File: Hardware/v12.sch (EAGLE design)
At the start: 82 parts, among them IC1 LM324D, IC2 m328p, IC3 REG1117, IC4 OPA336U, J1 22-27-2081-08, J2 22-27-2031-03

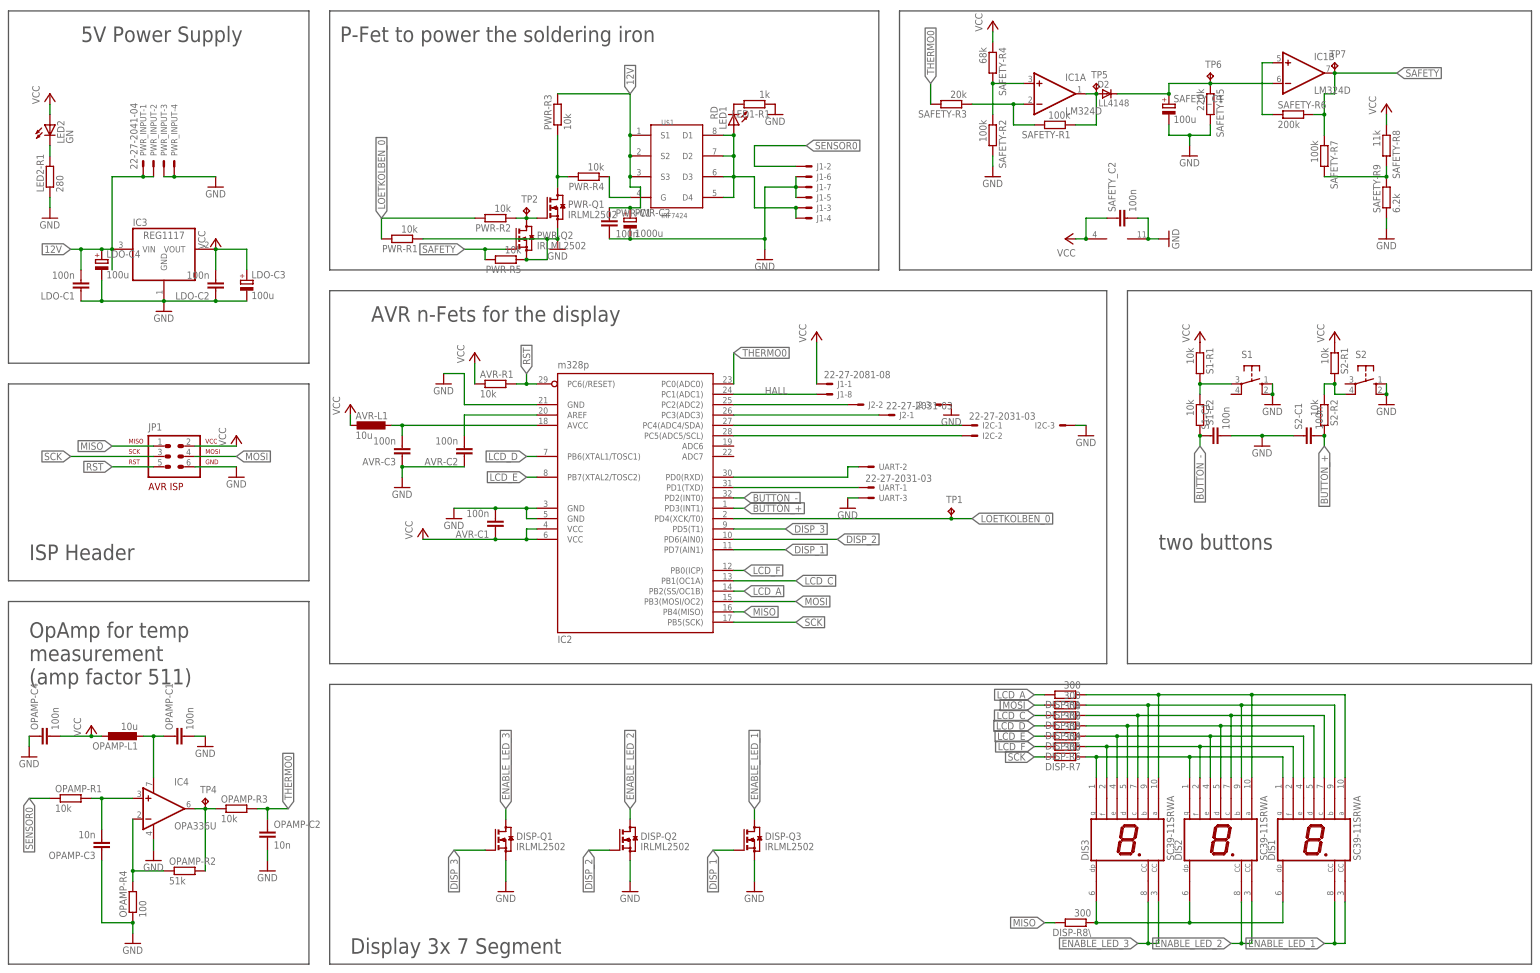
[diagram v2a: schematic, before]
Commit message: added silk screen to test points and optimized ground connections
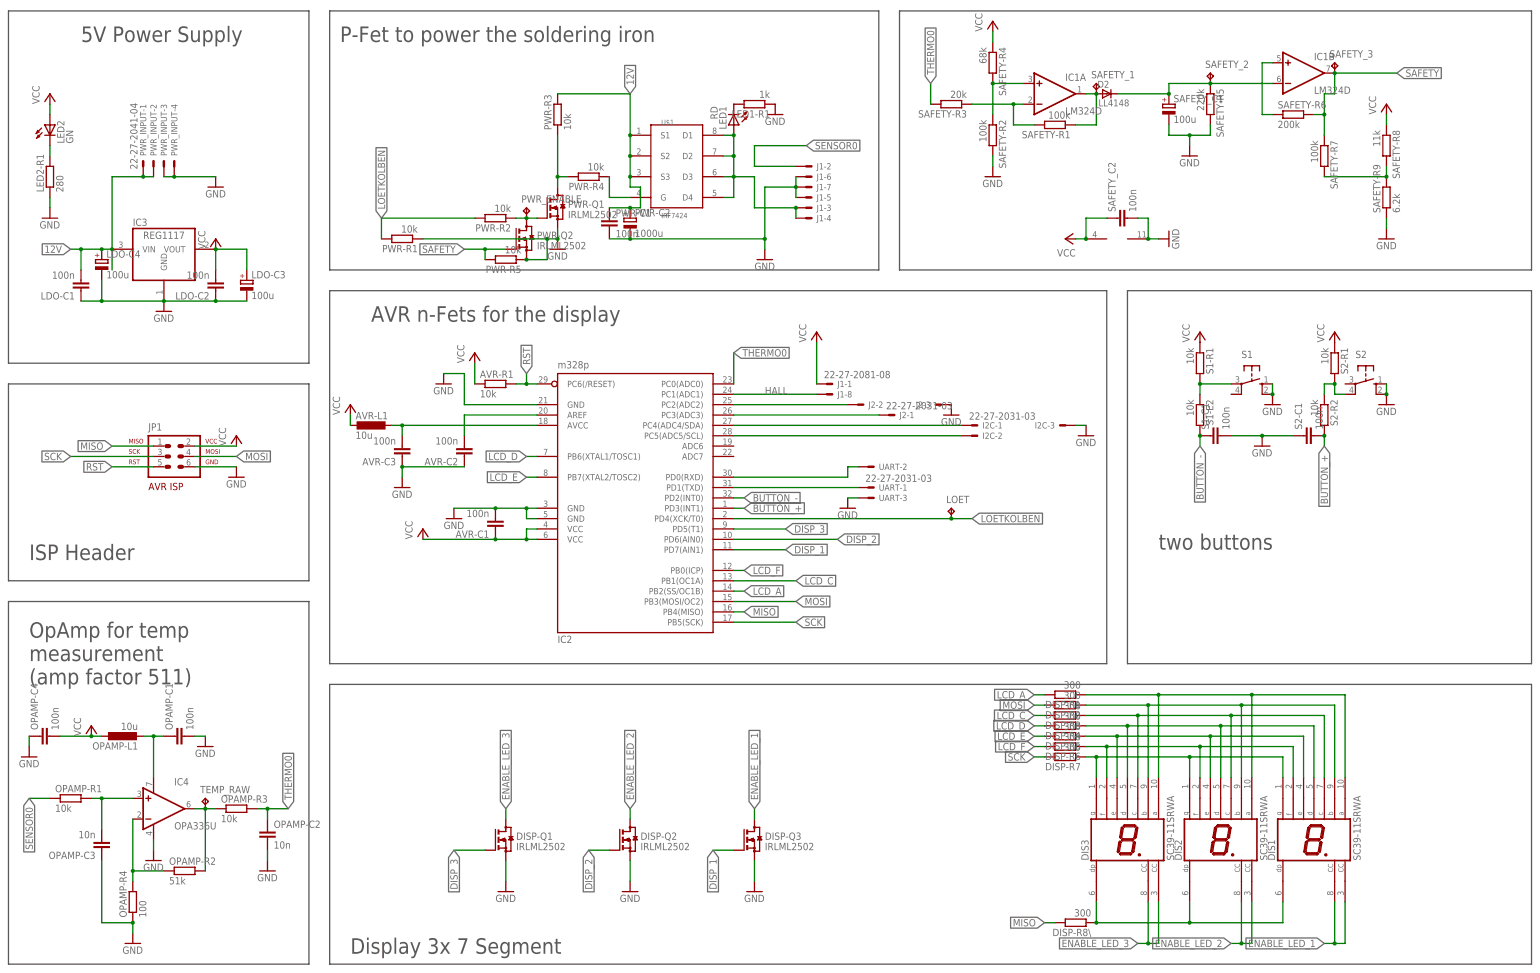
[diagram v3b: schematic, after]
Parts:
- renumbered TP1 to LOET, TP2 to PWR_ENABLE, TP4 to TEMP_RAW, TP5 to SAFETY_1, TP6 to SAFETY_2, TP7 to SAFETY_3
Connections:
- net LOETKOLBEN_0 renamed LOETKOLBEN
- net N$10 renamed TX
- net N$13 renamed PC2
- net N$2 renamed SDA
- net N$3 renamed PC3
- net N$4 renamed SCL
- net N$9 renamed RX
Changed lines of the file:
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@@
 <part name="J2" library="con-molex" deviceset="22-?-03" device="27-2031"/>
 <part name="GND28" library="supply1" deviceset="GND" device=""/>
-<part name="TP1" library="testpad" deviceset="TP" device="B1,27"/>
-<part name="TP2" library="testpad" deviceset="TP" device="B1,27"/>
-<part name="TP4" library="testpad" deviceset="TP" device="B1,27"/>
-<part name="TP5" library="testpad" deviceset="TP" device="B1,27"/>
-<part name="TP6" library="testpad" deviceset="TP" device="B1,27"/>
-<part name="TP7" library="testpad" deviceset="TP" device="B1,27"/>
+<part name="LOET" library="testpad" deviceset="TP" device="B1,27"/>
+<part name="PWR_ENABLE" library="testpad" deviceset="TP" device="B1,27"/>
+<part name="TEMP_RAW" library="testpad" deviceset="TP" device="B1,27"/>
+<part name="SAFETY_1" library="testpad" deviceset="TP" device="B1,27"/>
+<part name="SAFETY_2" library="testpad" deviceset="TP" device="B1,27"/>
+<part name="SAFETY_3" library="testpad" deviceset="TP" device="B1,27"/>
 <part name="D2" library="_hhn_diodes_smd" deviceset="LL4148" device=""/>
 </parts>
@@
 <instance part="J2" gate="-3" x="254" y="165.1" rot="R180"/>
 <instance part="GND28" gate="1" x="256.54" y="162.56"/>
-<instance part="TP1" gate="G$1" x="256.54" y="139.7"/>
-<instance part="TP2" gate="G$1" x="152.4" y="213.36"/>
-<instance part="TP4" gate="G$1" x="73.66" y="68.58"/>
-<instance part="TP5" gate="G$1" x="292.1" y="243.84"/>
-<instance part="TP6" gate="G$1" x="320.04" y="246.38"/>
-<instance part="TP7" gate="G$1" x="350.52" y="248.92"/>
+<instance part="LOET" gate="G$1" x="256.54" y="139.7"/>
+<instance part="PWR_ENABLE" gate="G$1" x="152.4" y="213.36"/>
+<instance part="TEMP_RAW" gate="G$1" x="73.66" y="68.58"/>
+<instance part="SAFETY_1" gate="G$1" x="292.1" y="243.84"/>
+<instance part="SAFETY_2" gate="G$1" x="320.04" y="246.38"/>
+<instance part="SAFETY_3" gate="G$1" x="350.52" y="248.92"/>
 <instance part="D2" gate="G$1" x="294.64" y="241.3"/>
 </instances>
@@
 </segment>
 </net>
-<net name="LOETKOLBEN_0" class="0">
+<net name="LOETKOLBEN" class="0">
 <segment>
 <pinref part="PWR-R1" gate="G$1" pin="2"/>
@@
 <pinref part="IC2" gate="G$1" pin="PD4(XCK/T0)"/>
 <wire x1="203.2" y1="137.16" x2="256.54" y2="137.16" width="0.1524" layer="91"/>
-<pinref part="TP1" gate="G$1" pin="TP"/>
+<pinref part="LOET" gate="G$1" pin="TP"/>
 <wire x1="256.54" y1="137.16" x2="261.62" y2="137.16" width="0.1524" layer="91"/>
 <junction x="256.54" y="137.16"/>
@@
 <wire x1="152.4" y1="210.82" x2="149.86" y2="210.82" width="0.1524" layer="91"/>
 <junction x="152.4" y="210.82"/>
-<pinref part="TP2" gate="G$1" pin="TP"/>
+<pinref part="PWR_ENABLE" gate="G$1" pin="TP"/>
 </segment>
 </net>
@@
 <pinref part="OPAMP-R3" gate="G$1" pin="1"/>
 <pinref part="IC4" gate="G$1" pin="OUT"/>
-<pinref part="TP4" gate="G$1" pin="TP"/>
+<pinref part="TEMP_RAW" gate="G$1" pin="TP"/>
 </segment>
 </net>
@@
 <junction x="350.52" y="246.38"/>
 <label x="365.76" y="246.38" size="1.778" layer="95" xref="yes"/>
-<pinref part="TP7" gate="G$1" pin="TP"/>
+<pinref part="SAFETY_3" gate="G$1" pin="TP"/>
 </segment>
 </net>
@@
 <wire x1="287.02" y1="233.68" x2="292.1" y2="233.68" width="0.1524" layer="91"/>
 <junction x="292.1" y="241.3"/>
-<pinref part="TP5" gate="G$1" pin="TP"/>
+<pinref part="SAFETY_1" gate="G$1" pin="TP"/>
 <pinref part="D2" gate="G$1" pin="A"/>
 </segment>
@@
 <pinref part="IC1" gate="B" pin="-IN"/>
 <wire x1="320.04" y1="243.84" x2="335.28" y2="243.84" width="0.1524" layer="91"/>
-<pinref part="TP6" gate="G$1" pin="TP"/>
+<pinref part="SAFETY_2" gate="G$1" pin="TP"/>
 <pinref part="D2" gate="G$1" pin="C"/>
 </segment>
@@
 </segment>
 </net>
-<net name="N$2" class="0">
+<net name="SDA" class="0">
 <segment>
 <pinref part="IC2" gate="G$1" pin="PC4(ADC4/SDA)"/>
@@
 </segment>
 </net>
-<net name="N$4" class="0">
+<net name="SCL" class="0">
 <segment>
 <pinref part="IC2" gate="G$1" pin="PC5(ADC5/SCL)"/>
@@
 </segment>
 </net>
-<net name="N$9" class="0">
+<net name="RX" class="0">
 <segment>
 <pinref part="IC2" gate="G$1" pin="PD0(RXD)"/>
@@
 </segment>
 </net>
-<net name="N$10" class="0">
+<net name="TX" class="0">
 <segment>
 <pinref part="IC2" gate="G$1" pin="PD1(TXD)"/>
@@
 </segment>
 </net>
-<net name="N$3" class="0">
+<net name="PC3" class="0">
 <segment>
 <pinref part="IC2" gate="G$1" pin="PC3(ADC3)"/>
@@
 </segment>
 </net>
-<net name="N$13" class="0">
+<net name="PC2" class="0">
 <segment>
 <pinref part="IC2" gate="G$1" pin="PC2(ADC2)"/>

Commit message: software readout of safety circuit additional led displaying state of safety circuit connecting soldering tip power switch to timer output OC0B
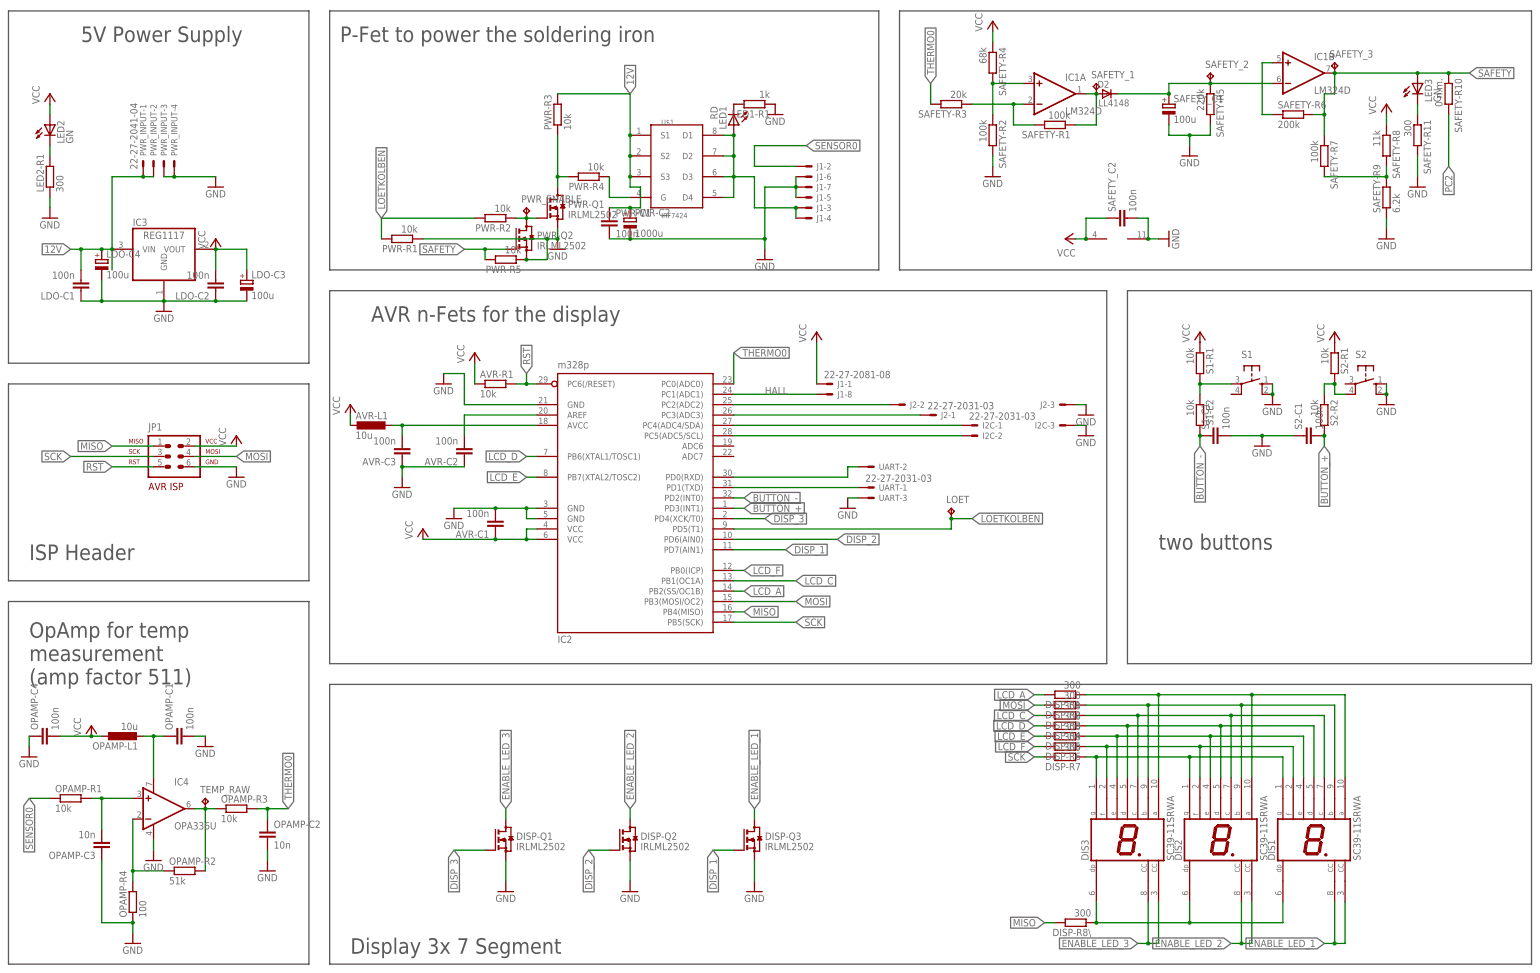
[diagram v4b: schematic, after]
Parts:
- added LED3: GN, led:LEDCHIP-LED0805
- added SAFETY-R10: 0 n.m., rcl:R-EU_R0603
- added SAFETY-R11: 300, rcl:R-EU_R0603
- LED2-R1: value 280 -> 300
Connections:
- new net N$2: LED3.C, SAFETY-R11.1
- net DISP_3: now also IC2.PD4(XCK/T0); no longer IC2.PD5(T1)
- net GND: now also SAFETY-R11.2
- net LOETKOLBEN: now also IC2.PD5(T1); no longer IC2.PD4(XCK/T0)
- net PC2: now also SAFETY-R10.2
- net SAFETY: now also LED3.A, SAFETY-R10.1
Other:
- moved on the sheet: J2-1, J2-2, J2-3
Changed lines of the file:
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@@
 <part name="P+8" library="supply1" deviceset="VCC" device=""/>
 <part name="LED2" library="led" deviceset="LED" device="CHIP-LED0805" value="GN"/>
-<part name="LED2-R1" library="rcl" deviceset="R-EU_" device="R0603" value="280"/>
+<part name="LED2-R1" library="rcl" deviceset="R-EU_" device="R0603" value="300"/>
 <part name="GND20" library="supply1" deviceset="GND" device=""/>
 <part name="P+9" library="supply1" deviceset="VCC" device=""/>
@@
 <part name="SAFETY_3" library="testpad" deviceset="TP" device="B1,27"/>
 <part name="D2" library="_hhn_diodes_smd" deviceset="LL4148" device=""/>
+<part name="SAFETY-R10" library="rcl" deviceset="R-EU_" device="R0603" value="0 n.m."/>
+<part name="LED3" library="led" deviceset="LED" device="CHIP-LED0805" value="GN"/>
+<part name="SAFETY-R11" library="rcl" deviceset="R-EU_" device="R0603" value="300"/>
+<part name="GND29" library="supply1" deviceset="GND" device=""/>
 </parts>
 <sheets>
@@
 <instance part="OPAMP-C4" gate="G$1" x="33.02" y="83.82" rot="R90"/>
 <instance part="GND1" gate="1" x="30.48" y="78.74"/>
-<instance part="J2" gate="-1" x="241.3" y="162.56"/>
-<instance part="J2" gate="-2" x="233.68" y="165.1"/>
-<instance part="J2" gate="-3" x="254" y="165.1" rot="R180"/>
-<instance part="GND28" gate="1" x="256.54" y="162.56"/>
+<instance part="J2" gate="-1" x="251.46" y="162.56"/>
+<instance part="J2" gate="-2" x="243.84" y="165.1"/>
+<instance part="J2" gate="-3" x="284.48" y="165.1" rot="R180"/>
+<instance part="GND28" gate="1" x="289.56" y="162.56"/>
 <instance part="LOET" gate="G$1" x="256.54" y="139.7"/>
 <instance part="PWR_ENABLE" gate="G$1" x="152.4" y="213.36"/>
@@
 <instance part="SAFETY_3" gate="G$1" x="350.52" y="248.92"/>
 <instance part="D2" gate="G$1" x="294.64" y="241.3"/>
+<instance part="SAFETY-R10" gate="G$1" x="378.46" y="241.3" rot="R270"/>
+<instance part="LED3" gate="G$1" x="370.84" y="243.84"/>
+<instance part="SAFETY-R11" gate="G$1" x="370.84" y="231.14" rot="R270"/>
+<instance part="GND29" gate="1" x="370.84" y="218.44"/>
 </instances>
 <busses>
@@
 <pinref part="J2" gate="-3" pin="S"/>
 <pinref part="GND28" gate="1" pin="GND"/>
+<wire x1="289.56" y1="165.1" x2="287.02" y2="165.1" width="0.1524" layer="91"/>
+</segment>
+<segment>
+<pinref part="SAFETY-R11" gate="G$1" pin="2"/>
+<pinref part="GND29" gate="1" pin="GND"/>
+<wire x1="370.84" y1="220.98" x2="370.84" y2="226.06" width="0.1524" layer="91"/>
 </segment>
 </net>
@@
 <segment>
 <label x="261.62" y="137.16" size="1.778" layer="95" xref="yes"/>
-<pinref part="IC2" gate="G$1" pin="PD4(XCK/T0)"/>
-<wire x1="203.2" y1="137.16" x2="256.54" y2="137.16" width="0.1524" layer="91"/>
 <pinref part="LOET" gate="G$1" pin="TP"/>
 <wire x1="256.54" y1="137.16" x2="261.62" y2="137.16" width="0.1524" layer="91"/>
+<wire x1="256.54" y1="137.16" x2="256.54" y2="134.62" width="0.1524" layer="91"/>
 <junction x="256.54" y="137.16"/>
+<pinref part="IC2" gate="G$1" pin="PD5(T1)"/>
+<wire x1="256.54" y1="134.62" x2="203.2" y2="134.62" width="0.1524" layer="91"/>
 </segment>
 </net>
@@
 </segment>
 <segment>
-<pinref part="IC2" gate="G$1" pin="PD5(T1)"/>
-<wire x1="203.2" y1="134.62" x2="215.9" y2="134.62" width="0.1524" layer="91"/>
-<label x="215.9" y="134.62" size="1.778" layer="95" xref="yes"/>
+<pinref part="IC2" gate="G$1" pin="PD4(XCK/T0)"/>
+<wire x1="210.82" y1="137.16" x2="203.2" y2="137.16" width="0.1524" layer="91"/>
+<label x="210.82" y="137.16" size="1.778" layer="95" xref="yes"/>
 </segment>
 </net>
@@
 <pinref part="IC1" gate="B" pin="OUT"/>
 <wire x1="350.52" y1="241.3" x2="350.52" y2="246.38" width="0.1524" layer="91"/>
-<wire x1="350.52" y1="246.38" x2="365.76" y2="246.38" width="0.1524" layer="91"/>
+<wire x1="350.52" y1="246.38" x2="370.84" y2="246.38" width="0.1524" layer="91"/>
 <junction x="350.52" y="246.38"/>
-<label x="365.76" y="246.38" size="1.778" layer="95" xref="yes"/>
+<label x="383.54" y="246.38" size="1.778" layer="95" xref="yes"/>
 <pinref part="SAFETY_3" gate="G$1" pin="TP"/>
+<pinref part="SAFETY-R10" gate="G$1" pin="1"/>
+<wire x1="370.84" y1="246.38" x2="378.46" y2="246.38" width="0.1524" layer="91"/>
+<wire x1="378.46" y1="246.38" x2="383.54" y2="246.38" width="0.1524" layer="91"/>
+<junction x="378.46" y="246.38"/>
+<pinref part="LED3" gate="G$1" pin="A"/>
+<junction x="370.84" y="246.38"/>
 </segment>
 </net>
@@
 <pinref part="IC2" gate="G$1" pin="PC3(ADC3)"/>
 <pinref part="J2" gate="-1" pin="S"/>
-<wire x1="238.76" y1="162.56" x2="203.2" y2="162.56" width="0.1524" layer="91"/>
+<wire x1="248.92" y1="162.56" x2="203.2" y2="162.56" width="0.1524" layer="91"/>
 </segment>
 </net>
@@
 <pinref part="IC2" gate="G$1" pin="PC2(ADC2)"/>
 <pinref part="J2" gate="-2" pin="S"/>
-<wire x1="231.14" y1="165.1" x2="203.2" y2="165.1" width="0.1524" layer="91"/>
-</segment>
-</net>
+<wire x1="241.3" y1="165.1" x2="203.2" y2="165.1" width="0.1524" layer="91"/>
+</segment>
+<segment>
+<pinref part="SAFETY-R10" gate="G$1" pin="2"/>
+<wire x1="378.46" y1="223.52" x2="378.46" y2="236.22" width="0.1524" layer="91"/>
+<label x="378.46" y="223.52" size="1.778" layer="95" rot="R270" xref="yes"/>
+</segment>
+</net>
+<net name="N$2" class="0">
+<segment>
+<pinref part="LED3" gate="G$1" pin="C"/>
+<pinref part="SAFETY-R11" gate="G$1" pin="1"/>
+<wire x1="370.84" y1="236.22" x2="370.84" y2="238.76" width="0.1524" layer="91"/>
+</segment>
+</net>
